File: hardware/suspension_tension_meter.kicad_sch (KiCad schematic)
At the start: 18 parts, among them J1 Conn_01x04, J2 Conn_01x06, J3 Conn_01x04, J4 Conn_01x04, SW1 Tactswitch, U1 STM32L4P5RET6, Y1 16MHz

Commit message: Apply KiCad template to the project
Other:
- sheet Power Supply ports: added none; removed +24V, GND
- note added: "Load Cell 1"
- note added: "Load Cell 2"
- note added: "Power"
- note added: "Programmer"
- title: Push-rods Suspension Tension Meter -> Suspension Tension Meter
- moved on the sheet: J1, J2, J3, J4

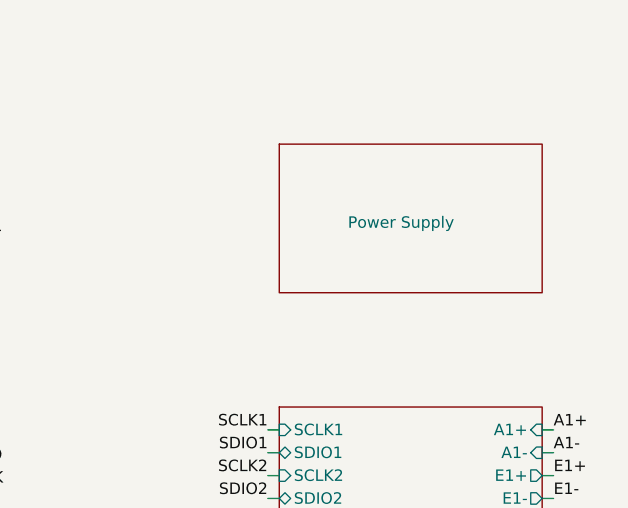
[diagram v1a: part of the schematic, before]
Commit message: Added new, debugged power supply, but the old one is still there, just in case
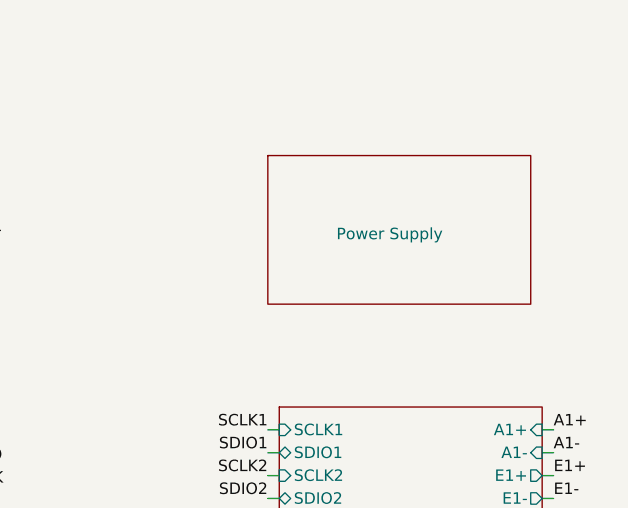
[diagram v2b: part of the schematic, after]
